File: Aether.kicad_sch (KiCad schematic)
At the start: 29 parts

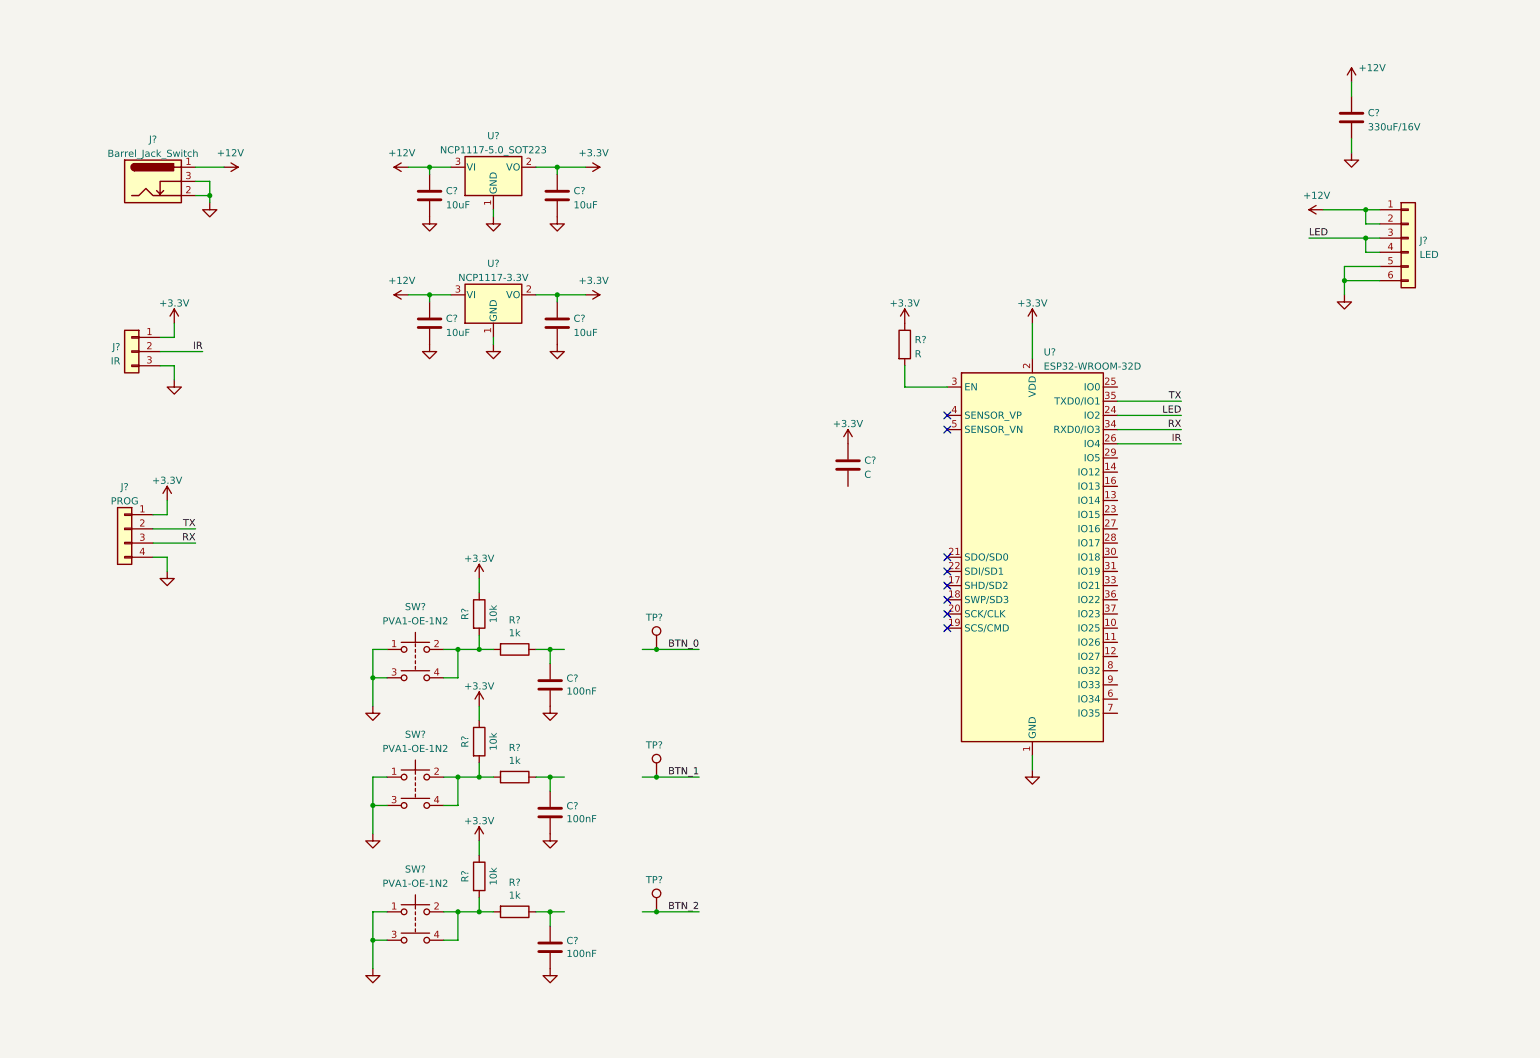
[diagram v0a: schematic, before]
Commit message: Schema: add level shifter, microphone and second LED output
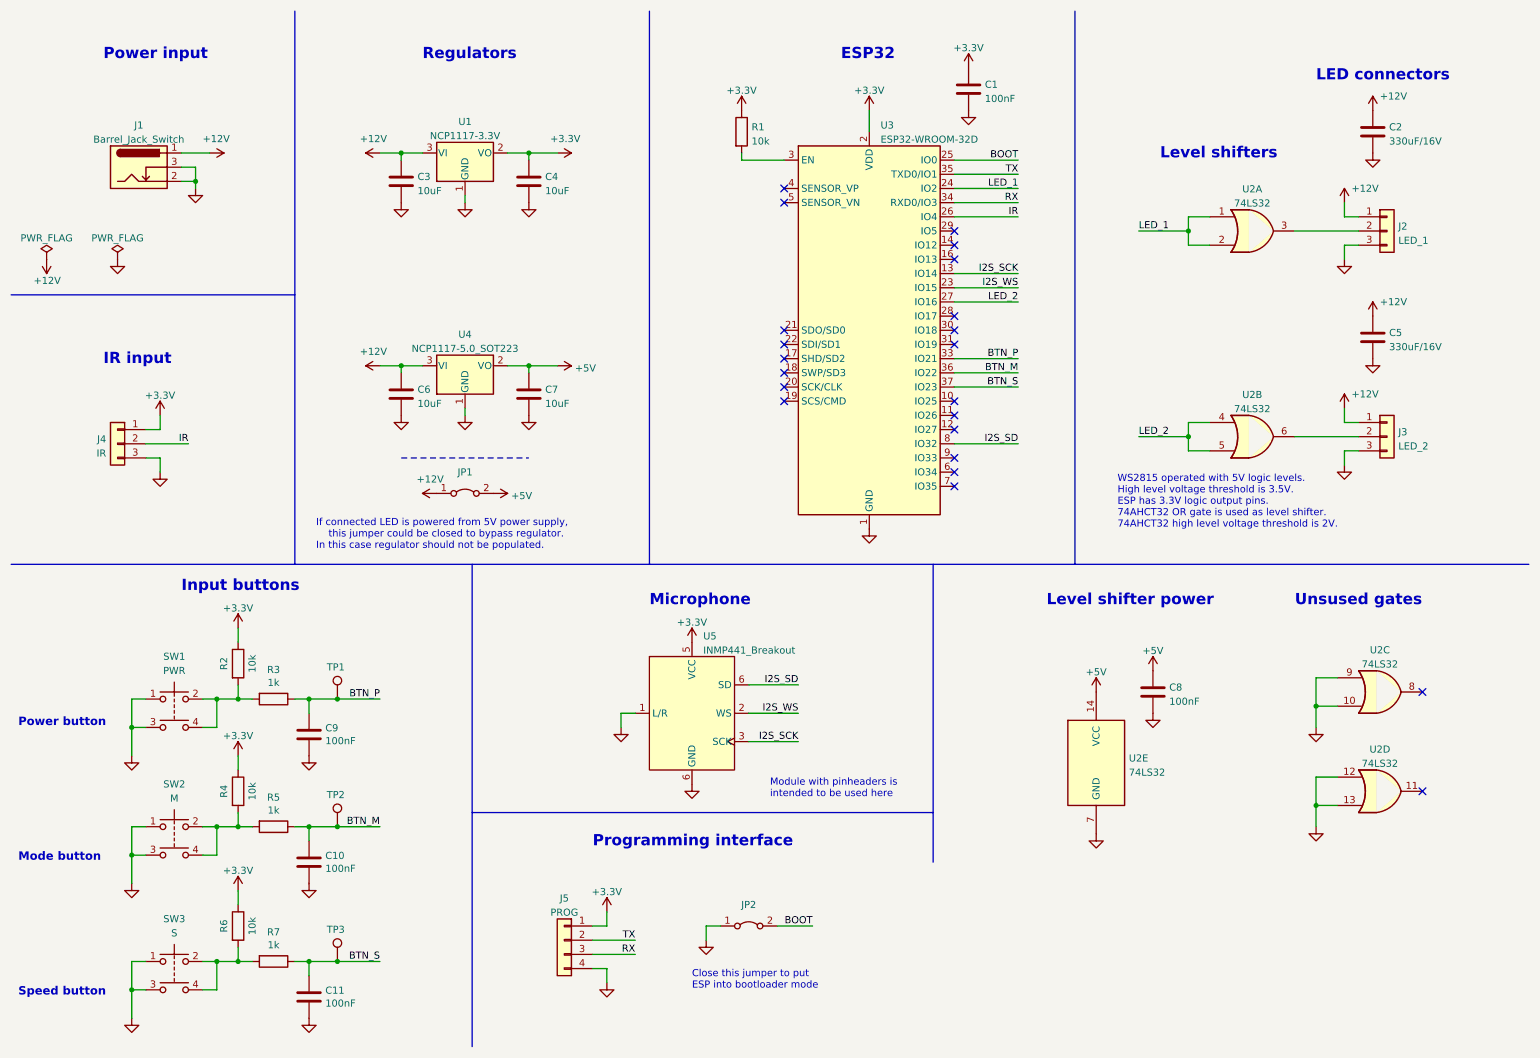
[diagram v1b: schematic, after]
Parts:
- removed C?: 330uF/16V, symbol Device:C
- removed J?: LED, symbol Connector_Generic:Conn_01x06
- added C2, C5: 330uF/16V, Capacitor_SMD:CP_Elec_8x10, symbol Device:C
- added C8: 100nF, TCY_passives:C_0603_1608Metric, symbol Device:C
- added J2: LED_1, Connector_PinHeader_2.54mm:PinHeader_1x03_P2.54mm_Vertical, symbol Connector_Generic:Conn_01x03
- added J3: LED_2, Connector_PinHeader_2.54mm:PinHeader_1x03_P2.54mm_Vertical, symbol Connector_Generic:Conn_01x03
- added JP1: 5V_PASSTHROUGH, Jumper:SolderJumper-2_P1.3mm_Open_RoundedPad1.0x1.5mm, symbol Jumper:Jumper_2_Bridged
- added JP2: BOOT, Connector_PinHeader_2.54mm:PinHeader_1x02_P2.54mm_Vertical, symbol Jumper:Jumper_2_Bridged
- added U2: 74LS32, Package_DFN_QFN:Texas_S-PVQFN-N14, symbol 74xx:74LS32
- added U5: INMP441_Breakout, TCY_sensors:INMP441_Breakout, symbol TCY_sensors:INMP441_Breakout
- C1: renamed from C?; value C -> 100nF; footprint (none) -> TCY_passives:C_0603_1608Metric
- C3, C4, C6, C7: renamed from C?; footprint (none) -> TCY_passives:C_0805_2012Metric
- J4: renamed from J?; footprint (none) -> Connector_PinHeader_2.54mm:PinHeader_1x03_P2.54mm_Vertical
- J5: renamed from J?; footprint (none) -> Connector_PinHeader_2.54mm:PinHeader_1x04_P2.54mm_Vertical
- R1: renamed from R?; value R -> 10k; footprint (none) -> TCY_passives:R_0603_1608Metric
- SW1: renamed from SW?; value PVA1-OE-1N2 -> PWR
- SW2: renamed from SW?; value PVA1-OE-1N2 -> M
- SW3: renamed from SW?; value PVA1-OE-1N2 -> S
- gave numbers to parts that had none: 16
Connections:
- net BTN_0 is gone; now on net BTN_P: TP1.1
- net BTN_1 is gone; now on net BTN_M: TP2.1
- net BTN_2 is gone; now on net BTN_S: TP3.1
- net +12V: now also C2.1, C5.1, J2.1 (Pin_1), J3.1 (Pin_1), JP1.1 (A)
- net GND: now also C1.2, C2.2, C5.2, C8.2, J2.3 (Pin_3), J3.3 (Pin_3), JP2.1 (A), U2.10, U2.12, U2.13, U2.7 (GND), U2.9, U5.1 (L/R), U5.6 (SD)
- net BTN_S: now reaches C11.1, R7.1
- net BTN_S: now also U3.37 (IO23)
- net BTN_P: now reaches C9.1, R3.1
- net BTN_P: now also U3.33 (IO21)
- net BTN_M: now reaches C10.1, R5.1
- net BTN_M: now also U3.36 (IO22)
- net I2S_SCK: now reaches U3.13 (IO14)
- net I2S_SCK: now also U5.3 (SCK)
- net I2S_WS: now reaches U3.23 (IO15)
- net I2S_WS: now also U5.2 (WS)
- net BOOT: now reaches U3.25 (IO0)
- net BOOT: now also JP2.2 (B)
- net LED_2: now reaches U3.27 (IO16)
- net LED_2: now also U2.4, U2.5
- net I2S_SD: now reaches U3.8 (IO32)
- net I2S_SD: now also U5.6 (SD)
- net +3V3 renamed +3.3V
- net +3.3V: now also U5.5 (VCC); no longer C7.1, U4.2 (VO)
- net LED renamed LED_1
- net LED_1: now also U2.1, U2.2
- new net: J2.2 (Pin_2), U2.3
- new net: J3.2 (Pin_2), U2.6
- new net +5V: C7.1, C8.1, JP1.2 (B), U2.14 (VCC), U4.2 (VO)
- no-connect marks 8 -> 22
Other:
- note added: "Close this jumper to put ESP into bootloader mode"
- note added: "ESP32"
- note added: "IR input"
- note added: "If connected LED is powered from 5V power supply, this jumper could be closed to bypass regulator. In this case regulator should not be populated."
- note added: "Input buttons"
- note added: "LED connectors"
- note added: "Level shifter power"
- note added: "Level shifters"
- note added: "Microphone"
- note added: "Mode button"
- note added: "Module with pinheaders is intended to be used here"
- note added: "Power button"
- note added: "Power input"
- note added: "Programming interface"
- note added: "Regulators"
- note added: "Speed button"
- note added: "Unsused gates"
- note added: "WS2815 operated with 5V logic levels. High level voltage threshold is 3.5V. ESP has 3.3V logic output pins. 74AHCT32 OR gate is used as level shifter. 74AHCT32 high level voltage threshold is 2V."
- company: (none) -> Author: Petr Malaník
- title: (none) -> Aether
- moved on the sheet: C1, C10, C11, C3, C4, C6, C7, C9, J1, J4, J5, R1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

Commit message: Schema: add microphone, mounting holes and finalize buttons
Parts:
- removed TP1, TP2, TP3: TestPoint, TestPoint:TestPoint_Pad_D1.0mm, symbol Connector:TestPoint
- removed U5: INMP441_Breakout, TCY_sensors:INMP441_Breakout, symbol TCY_sensors:INMP441_Breakout
- added C12: 100nF, TCY_passives:C_0603_1608Metric, symbol Device:C
- added H1, H2, H3, H4: M2, MountingHole:MountingHole_2.2mm_M2_Pad_Via, symbol Mechanical:MountingHole_Pad
- added R8: 100k, TCY_passives:R_0603_1608Metric, symbol Device:R
- added U5: INMP441, TCY_sensors:INMP441, symbol TCY_sensors:INMP441
- C2, C5: footprint Capacitor_SMD:CP_Elec_8x10 -> Capacitor_SMD:CP_Elec_6.3x7.7
- J1: footprint (none) -> TCY_connectors:Barrel_jack_short
- J5: footprint Connector_PinHeader_2.54mm:PinHeader_1x04_P2.54mm_Vertical -> Connector_PinHeader_2.54mm:PinHeader_1x03_P2.54mm_Vertical; symbol Connector_Generic:Conn_01x04 -> Connector_Generic:Conn_01x03
- SW1, SW2, SW3: footprint TCY_connectors:PVA-Button -> Button_Switch_SMD:SW_SPST_TL3342; symbol Switch:SW_Push_Dual -> Switch:SW_Push
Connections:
- net +3.3V: now also C12.1, U5.6 (VCC), U5.7 (CHIP_EN); no longer J5.1 (Pin_1)
- net GND: now also J5.3 (Pin_3), C12.2, H1.1, H2.1, H3.1, H4.1, R8.2, U5.4 (L/R), U5.5 (GND), U5.8 (GND), U5.9 (GND); no longer J5.4 (Pin_4), SW1.3, SW2.3, SW3.3
- net I2S_SCK: now also U5.1 (SCK)
- net I2S_SD: now also R8.1, U5.2 (SD)
- net I2S_WS: now also U5.3 (WS)
- net LED_1: now also U2.4, U2.5; no longer U2.1, U2.2
- net LED_2: now also U2.1, U2.2; no longer U2.4, U2.5
- net RX: now also J5.2 (Pin_2); no longer J5.3 (Pin_3)
- net TX: now also J5.1 (Pin_1); no longer J5.2 (Pin_2)
- net at R6.2, R7.2, SW3.2: no longer SW3.4
- net at R4.2, R5.2, SW2.2: no longer SW2.4
- net at U2.3: now also J3.2 (Pin_2); no longer J2.2 (Pin_2)
- net at U2.6: now also J2.2 (Pin_2); no longer J3.2 (Pin_2)
- net at R2.2, R3.2, SW1.2: no longer SW1.4
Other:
- note added: "Decoupling"
- note added: "Mounting Holes"
- moved on the sheet: C8, U2A, U2B, U2C, U2D, U2E
